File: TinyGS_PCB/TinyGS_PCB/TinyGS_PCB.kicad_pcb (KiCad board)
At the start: 2 copper layers, 45.7 x 119.4 mm, 6 parts, among them J1 Power Input, U1 ESP32, U2 E32400M30S, U3 OLED

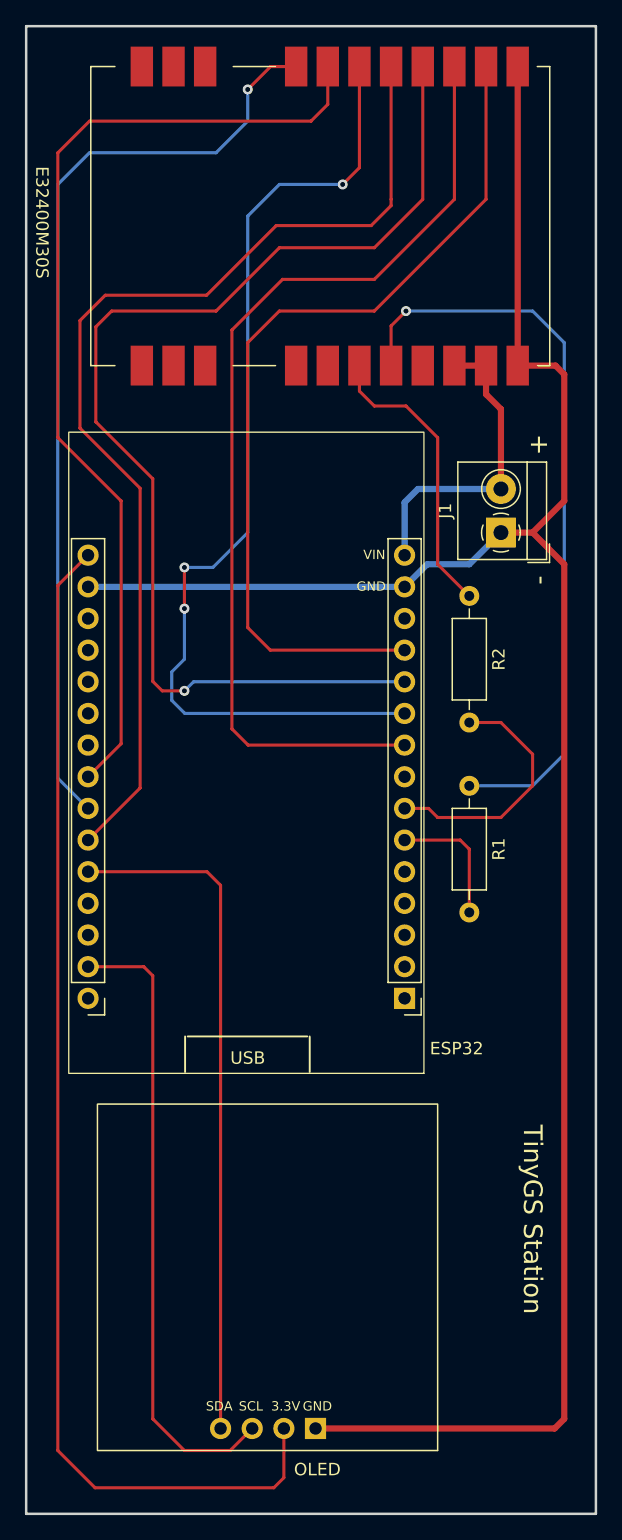
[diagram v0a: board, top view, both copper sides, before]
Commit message: Added the software change needed for the SX1278 chip to get work with tinygs
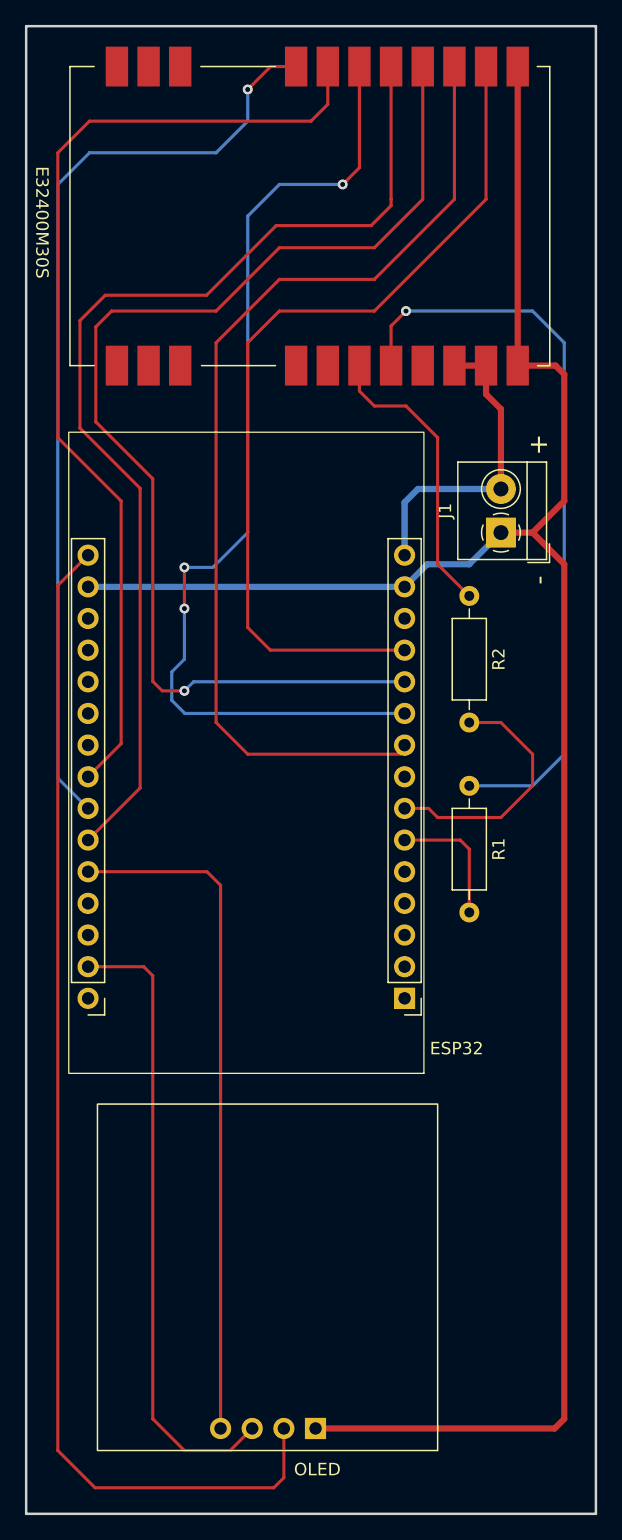
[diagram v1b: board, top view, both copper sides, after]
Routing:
- net Net-(U1-Pad9): track 79.3 -> 82.1 mm
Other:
- board text removed: "3.3V"
- board text removed: "GND"
- board text removed: "SCL"
- board text removed: "SDA"
- board text removed: "SpicySpaceCraft"
- board text removed: "TinyGS Station"
- board text removed: "USB"
- board text removed: "VIN"
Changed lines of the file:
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@@
       (drillshape 0)
       (scaleselection 1)
-      (outputdirectory "gerber_final/")
+      (outputdirectory "")
     )
   )
@@
       (effects (font (size 1 1) (thickness 0.15)))
     )
-    (fp_line (start 0 22) (end 0 25.4) (layer "F.SilkS") (width 0.12))
-    (fp_line (start 24 36.83) (end 24 34.89) (layer "F.SilkS") (width 0.12))
-    (fp_line (start 24 22) (end 24 25.4) (layer "F.SilkS") (width 0.12))
+    (fp_line (start 24 38.5) (end 24 36.56) (layer "F.SilkS") (width 0.12))
+    (fp_line (start 0 38.5) (end 0 36.56) (layer "F.SilkS") (width 0.12))
+    (fp_line (start 0 22) (end 0 28) (layer "F.SilkS") (width 0.12))
     (fp_line (start 24 0) (end 24 1) (layer "F.SilkS") (width 0.12))
-    (fp_line (start 0 36.83) (end 24 36.83) (layer "F.SilkS") (width 0.12))
     (fp_line (start 0 0) (end 0 1) (layer "F.SilkS") (width 0.12))
-    (fp_line (start 0 36.83) (end 0 34.89) (layer "F.SilkS") (width 0.12))
+    (fp_line (start 0 38.5) (end 24 38.5) (layer "F.SilkS") (width 0.12))
     (fp_line (start 0 0) (end 24 0) (layer "F.SilkS") (width 0.12))
-    (pad "1" smd rect (at 24 32.731 270) (size 3.2 1.8) (layers "F.Cu" "F.Paste" "F.Mask")
+    (fp_line (start 24 22) (end 24 27.94) (layer "F.SilkS") (width 0.12))
+    (pad "1" smd rect (at 24 34.731 270) (size 3.2 1.8) (layers "F.Cu" "F.Paste" "F.Mask")
       (net 32 "unconnected-(U2-Pad1)") (pinfunction "GND") (pintype "input"))
-    (pad "2" smd rect (at 24 30.191 270) (size 3.2 1.8) (layers "F.Cu" "F.Paste" "F.Mask")
+    (pad "2" smd rect (at 24 32.191 270) (size 3.2 1.8) (layers "F.Cu" "F.Paste" "F.Mask")
       (net 33 "unconnected-(U2-Pad2)") (pinfunction "GND") (pintype "input"))
-    (pad "3" smd rect (at 24 27.651 270) (size 3.2 1.8) (layers "F.Cu" "F.Paste" "F.Mask")
+    (pad "3" smd rect (at 24 29.651 270) (size 3.2 1.8) (layers "F.Cu" "F.Paste" "F.Mask")
       (net 34 "unconnected-(U2-Pad3)") (pinfunction "GND") (pintype "input"))
     (pad "4" smd rect (at 24 20.351 270) (size 3.2 1.8) (layers "F.Cu" "F.Paste" "F.Mask")
@@
     (pad "25" smd rect (at 0 20.351 270) (size 3.2 1.8) (layers "F.Cu" "F.Paste" "F.Mask")
       (net 25 "Net-(U1-Pad24)") (pinfunction "NSS") (pintype "input"))
-    (pad "26" smd rect (at 0 27.651 270) (size 3.2 1.8) (layers "F.Cu" "F.Paste" "F.Mask")
+    (pad "26" smd rect (at 0 29.651 270) (size 3.2 1.8) (layers "F.Cu" "F.Paste" "F.Mask")
       (net 38 "unconnected-(U2-Pad26)") (pinfunction "GND") (pintype "input"))
-    (pad "27" smd rect (at 0 30.191 270) (size 3.2 1.8) (layers "F.Cu" "F.Paste" "F.Mask")
+    (pad "27" smd rect (at 0 32.191 270) (size 3.2 1.8) (layers "F.Cu" "F.Paste" "F.Mask")
       (net 39 "unconnected-(U2-Pad27)") (pinfunction "ANT") (pintype "input"))
-    (pad "28" smd rect (at 0 32.731 270) (size 3.2 1.8) (layers "F.Cu" "F.Paste" "F.Mask")
+    (pad "28" smd rect (at 0 34.731 270) (size 3.2 1.8) (layers "F.Cu" "F.Paste" "F.Mask")
       (net 40 "unconnected-(U2-Pad28)") (pinfunction "GND") (pintype "input"))
-    (group "" (id 141bfae7-43cf-462e-bdc5-5b863d566990)
+    (group "" (id bdb7f77d-9184-44d6-bab7-cbf6b0704cdd)
       (members
-        54e38abe-961b-4810-af39-91ec6064011c
-        70b352b8-618a-4837-8232-d9fdcd6f5e24
-        eaab2938-b4f3-4ebb-ba61-9bb6382be53e
+        281db05e-45e8-4708-8a8a-46582d1874c2
+        2b104cfc-684f-4045-a215-6c25871ff13b
+        37490d11-710c-42b1-84e6-4b6d85cdd2fa
+        4d779715-9166-421e-9e46-c7f629c7857e
+        73ec31ed-9895-4a47-a1dd-70d83acaa674
+        755f125f-23e8-4f9f-939c-26d16ca9348a
+        76d93c0d-a184-46a0-a3e1-191d212e09b4
+        786bbd47-ba67-40d8-af7c-f76bae728b5e
+        8020e638-2392-4228-9de7-4e844bd1348d
+        f1570622-0c6b-4b0a-8aa9-a04b880717fe
+        f6187a2d-0f39-4718-8425-9db780b0082c
       )
     )
-    (group "" (id 8ebec0f4-9cf0-478e-9925-ccb4a4b6a462)
+    (group "" (id e1949532-9de6-4956-80ac-447056737088)
       (members
-        13227acf-563c-40f9-ad4e-139f8f7d53fc
-        27de8649-24cb-47da-96b0-4d28336aac86
-        28e0b73c-6e7d-4da2-ad6f-d689350d1c4e
-        46ddc337-b58b-42bb-a3f0-23efd58509dd
-        5aa694d5-81d1-40b1-8c1c-6b3145125127
-        9133ae65-b777-47b9-8cf7-ef9a8f8e72b6
-        9912b5d8-b5cd-4325-8b22-85387c4cbddd
-        9a4356f9-377e-4115-b34b-38a31999a8cf
-        a86abd2a-3e28-4d24-9581-f0477b151b02
-        b369a26a-5453-4fef-92db-2b1a8e010279
-        fa470eab-e2de-43aa-8a9c-77fdb2f32920
-      )
-    )
-    (group "" (id f3f3e720-9b47-4579-a0fc-1a5545c9979e)
-      (members
-        03bb9b38-c09c-424f-9bc5-5068af64d38f
-        13e455ed-5a15-41d9-99a5-b70d8819ebd5
-        265e8abd-da46-4e26-9931-7cfea70adaed
-        27e29902-3294-40a4-b047-00788bfbef99
-        58d70f19-a01e-4244-9efa-b060ca8dfde1
-        61f6bf65-b581-41a0-9b05-c658009b7026
-        75658d12-f34f-4d65-95f3-54b607364d19
-        8e4a2ef7-0688-4f30-9191-1f8a036694d0
-        d994901b-3f30-41e9-9459-0604c555fdf4
-        eb8f6f9c-922e-4d58-94b9-0d81055e26be
-        f65cb95c-b361-4260-b24a-1b857cd0326a
+        1463b563-f57e-4f01-acf2-6ba2e5c67006
+        38a20560-757b-4722-9b33-d0611b36ebe6
+        3f404853-f298-467d-94c7-b624ae5a967a
+        48ba6ed2-0a0e-4b13-898d-82ebe239f85b
+        8feb8d3d-3776-4517-8c66-0e86794763d5
+        a6e8273b-13f8-4a5a-a615-9eadb8f12131
+        ab82d8af-c1da-44cd-8e4a-5cd280014ecc
+        ae1f26a1-4c5b-4ffc-94aa-c9891b5b99d1
+        b0713971-57b6-40b2-b0ca-e0f9d9038e41
+        cfe7624e-711c-4edd-8e1c-8f5987ad0d71
+        da194a04-bde7-430c-9dbe-d15944bad7cc
       )
     )
@@
     )
   )
-  (gr_line (start 116.894 111.55) (end 116.894 114.4) (layer "F.SilkS") (width 0.15))
-  (gr_line (start 126.894 111.55) (end 126.894 114.4) (layer "F.SilkS") (width 0.15))
-  (gr_line (start 117.1 111.55) (end 126.7 111.55) (layer "F.SilkS") (width 0.15))
   (gr_rect (start 149.86 149.86) (end 104.14 30.48) (layer "Edge.Cuts") (width 0.2) (fill none))
-  (gr_text "SpicySpaceCraft" (at 108.204 124.968 90) (layer "B.SilkS")
-    (effects (font (size 1.5 1.5) (thickness 0.3)) (justify mirror))
-  )
   (gr_text "+" (at 145.288 64.008) (layer "F.SilkS")
     (effects (font (size 1.5 1.5) (thickness 0.3)) (justify mirror))
   )
-  (gr_text "SCL\n" (at 122.174 141.224) (layer "F.SilkS")
-    (effects (font (size 0.75 0.75) (thickness 0.1875)))
-  )
-  (gr_text "3.3V\n" (at 124.968 141.224) (layer "F.SilkS")
-    (effects (font (size 0.75 0.75) (thickness 0.1875)))
-  )
-  (gr_text "GND\n" (at 131.826 75.438) (layer "F.SilkS")
-    (effects (font (size 0.75 0.75) (thickness 0.1875)))
-  )
-  (gr_text "TinyGS Station " (at 144.78 126.238 270) (layer "F.SilkS")
-    (effects (font (size 1.5 1.5) (thickness 0.3)))
-  )
   (gr_text "-" (at 145.288 74.93 90) (layer "F.SilkS")
     (effects (font (size 1.5 1.5) (thickness 0.3)) (justify mirror))
-  )
-  (gr_text "VIN\n" (at 132.08 72.898) (layer "F.SilkS")
-    (effects (font (size 0.75 0.75) (thickness 0.1875)))
-  )
-  (gr_text "SDA\n" (at 119.634 141.224) (layer "F.SilkS")
-    (effects (font (size 0.75 0.75) (thickness 0.1875)))
-  )
-  (gr_text "USB" (at 121.92 113.284) (layer "F.SilkS")
-    (effects (font (size 1 1) (thickness 0.15)))
-  )
-  (gr_text "GND" (at 127.508 141.224) (layer "F.SilkS")
-    (effects (font (size 0.75 0.75) (thickness 0.1875)))
   )
   (segment (start 147.32 68.58) (end 144.78 71.12) (width 0.5) (layer "F.Cu") (net 1))
@@
   (segment (start 144.78 91.44) (end 142.24 93.98) (width 0.25) (layer "F.Cu") (net 6))
   (segment (start 142.24 86.36) (end 144.78 88.9) (width 0.25) (layer "F.Cu") (net 6))
-  (segment (start 121.9545 88.1725) (end 134.5075 88.1725) (width 0.25) (layer "F.Cu") (net 13))
-  (segment (start 132.08 50.8) (end 124.714 50.8) (width 0.25) (layer "F.Cu") (net 13))
-  (segment (start 120.65 86.868) (end 121.9545 88.1725) (width 0.25) (layer "F.Cu") (net 13))
+  (segment (start 132.08 50.8) (end 124.46 50.8) (width 0.25) (layer "F.Cu") (net 13))
+  (segment (start 119.38 86.36) (end 121.92 88.9) (width 0.25) (layer "F.Cu") (net 13))
+  (segment (start 119.38 55.88) (end 119.38 86.36) (width 0.25) (layer "F.Cu") (net 13))
+  (segment (start 134.62 88.285) (end 134.5075 88.1725) (width 0.25) (layer "F.Cu") (net 13))
+  (segment (start 121.92 88.9) (end 134.62 88.9) (width 0.25) (layer "F.Cu") (net 13))
+  (segment (start 138.504 33.72) (end 138.504 44.376) (width 0.25) (layer "F.Cu") (net 13))
+  (segment (start 124.46 50.8) (end 119.38 55.88) (width 0.25) (layer "F.Cu") (net 13))
+  (segment (start 134.62 88.9) (end 134.62 88.285) (width 0.25) (layer "F.Cu") (net 13))
   (segment (start 138.504 44.376) (end 132.08 50.8) (width 0.25) (layer "F.Cu") (net 13))
-  (segment (start 138.504 33.72) (end 138.504 44.376) (width 0.25) (layer "F.Cu") (net 13))
-  (segment (start 124.714 50.8) (end 120.65 54.864) (width 0.25) (layer "F.Cu") (net 13))
-  (segment (start 120.65 54.864) (end 120.65 86.868) (width 0.25) (layer "F.Cu") (net 13))
   (segment (start 130.884 33.72) (end 130.884 41.836) (width 0.25) (layer "F.Cu") (net 14))
   (segment (start 130.884 41.836) (end 129.54 43.18) (width 0.25) (layer "F.Cu") (net 14))
